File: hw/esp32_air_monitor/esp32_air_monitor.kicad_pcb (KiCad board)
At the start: 2 copper layers, 155 x 60 mm, 7 parts, among them J1 Conn_01x02_Male, J2 Connector_LED_matrix_64x32, J3 Connector_LED_matrix_64x32, J4 Connector_Pimoroni_BME280, J5 Connector_Adafruit_VEML7700, U1 ESP32-DEVKITC-32D, U2 SCD30

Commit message: :)s
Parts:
- moved J4 2.41 mm to (143.8, 116.4)
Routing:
- net +3V3: track 137.4 -> 142.7 mm
- net /SDA: track 93.6 -> 97.1 mm
- net /SCL: track 127.6 -> 130.4 mm
- net +5V: track 122.2 -> 123.3 mm

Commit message: :)
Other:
- board text added: "JLCJLCJLCJLC"

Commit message: Update PCB
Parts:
- added R1: 10k, Resistor_SMD:R_1206_3216Metric_Pad1.30x1.75mm_HandSolder, F.Cu at (133.0, 93.7)
- added R2: 10k, Resistor_SMD:R_1206_3216Metric_Pad1.30x1.75mm_HandSolder, F.Cu at (96.9, 93.4)
- added R3: 10k, Resistor_SMD:R_1206_3216Metric_Pad1.30x1.75mm_HandSolder, F.Cu at (130.5, 93.7)
- added R4: 10k, Resistor_SMD:R_1206_3216Metric_Pad1.30x1.75mm_HandSolder, F.Cu at (127.9, 93.7)
- added R5: 10k, Resistor_SMD:R_1206_3216Metric_Pad1.30x1.75mm_HandSolder, F.Cu at (125.4, 93.7)
- added R6: 10k, Resistor_SMD:R_1206_3216Metric_Pad1.30x1.75mm_HandSolder, F.Cu at (106.5, 93.4)
- added R7: 10k, Resistor_SMD:R_1206_3216Metric_Pad1.30x1.75mm_HandSolder, F.Cu at (115.8, 93.4)
- added SW1: SW_Push, qc_attiny:Push_Button_6x6mm, F.Cu at (96.9, 88.0)
- added SW2: SW_Push, qc_attiny:Push_Button_6x6mm, F.Cu at (106.5, 88.0)
- added SW3: SW_Push, qc_attiny:Push_Button_6x6mm, F.Cu at (115.8, 88.0)
- added SW4: SW_DIP_x04, Button_Switch_THT:SW_DIP_SPSTx04_Slide_9.78x12.34mm_W7.62mm_P2.54mm, F.Cu at (125.4, 89.2)
- moved J4 53.1 mm to (187.3, 86.0)
- moved J1 42.1 mm to (143.9, 85.5), turned to 90 degrees
- moved J5 14.0 mm to (165.6, 119.7)
- moved J3 2.54 mm to (215.1, 93.4)
- moved U1 0.79 mm to (108.9, 113.7), turned to 270 degrees
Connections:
- J2 pad 2: /MOSI -> /R0
- J2 pad 8: /B1 -> /MOSI
- J3 pad 1: /G1 -> /R0
- J3 pad 2: /R1 -> (no net)
- J3 pad 4: /B1 -> /G0
- J3 pad 5: /B0 -> /R1
- J3 pad 6: /G0 -> /B0
- J3 pad 8: (no net) -> /G1
- U1 pad 10: (no net) -> /BUT_2
- U1 pad 11: (no net) -> /BUT_1
- U1 pad 21: /LINE_A -> (no net)
- U1 pad 22: /LINE_B -> /SDA
- U1 pad 23: (no net) -> /SCL
- U1 pad 25: /LINE_C -> (no net)
- U1 pad 27: /LINE_D -> (no net)
- U1 pad 28: /LATCH -> /LINE_B
- U1 pad 29: (no net) -> /LINE_D
- U1 pad 31: /OE -> (no net)
- U1 pad 32: /SCL -> /LINE_A
- U1 pad 33: (no net) -> /LINE_C
- U1 pad 34: (no net) -> /LATCH
- U1 pad 35: /SDA -> /OE
- U1 pad 5: (no net) -> /DIP_4
- U1 pad 6: (no net) -> /DIP_3
- U1 pad 7: (no net) -> /DIP_2
- U1 pad 8: (no net) -> /DIP_1
- U1 pad 9: (no net) -> /BUT_3
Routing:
- net /R0: track 0.00 -> 171.6 mm
- net /B1: track 143.5 -> 0.00 mm
- net /MOSI: track 94.4 -> 18.0 mm
- net /R1: track 143.6 -> 196.5 mm
- net +5V: track 123.3 -> 79.9 mm
- net /SCLK: track 67.2 -> 30.5 mm
- net /LINE_A: track 15.8 -> 50.7 mm
- net /G1: track 143.6 -> 174.6 mm
- net /SCL: track 130.4 -> 106.5 mm
- net /B0: track 166.4 -> 190.2 mm
- net /SDA: track 97.1 -> 119.8 mm, vias 0 -> 1
- net /DIP_1: track 0.00 -> 22.2 mm, vias 0 -> 1
- net /LINE_B: track 17.0 -> 39.2 mm
- net /DIP_3: track 0.00 -> 21.8 mm, vias 0 -> 1
- net /DIP_4: track 0.00 -> 21.8 mm, vias 0 -> 1
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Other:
- board text added: "Bosch BME280 T, RH, p sensor"
- board text added: "ESP32 air quality monitor (T, RH, p, CO2, Ev) Jan Vrhovec, 2021"
- board text added: "Espressif ESP32 Microcontroller"
- board text added: "Sensirion SCD30 CO2 sensor"
- board text added: "Vishay VEML7700 Ambient light sensor"
- board text removed: "ESP32 Air Quality Monitor (T, RH, p, CO2) Jan Vrhovec, 2020"

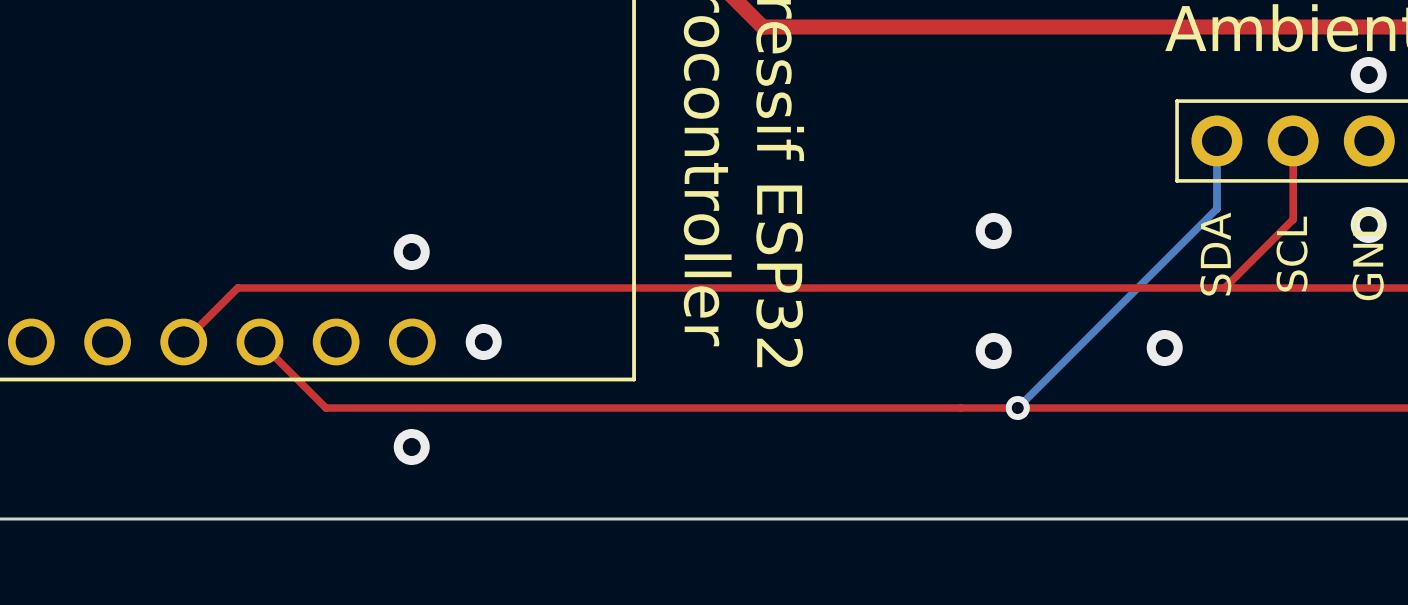
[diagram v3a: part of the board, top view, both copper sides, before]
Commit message: Fix hardware bug (SCL pin), patch software for new hw revision
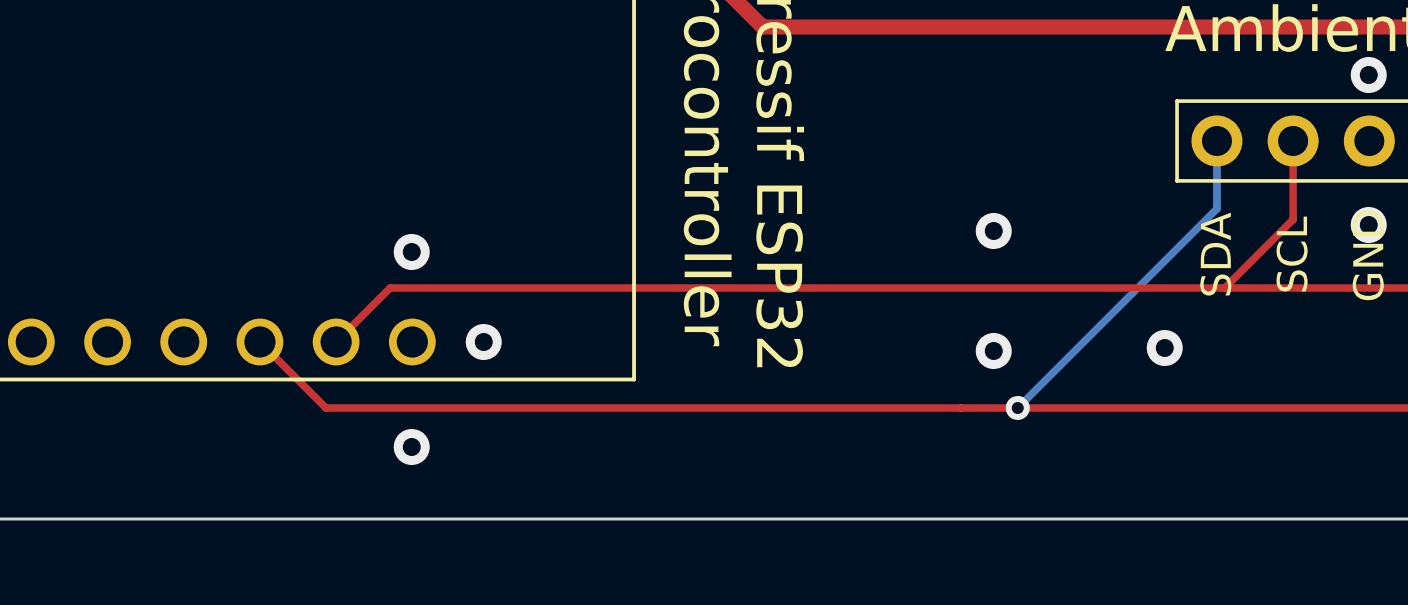
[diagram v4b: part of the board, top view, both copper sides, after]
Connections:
- U1 pad 21: (no net) -> /SCL
- U1 pad 23: /SCL -> (no net)
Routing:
- net /SCL: track 106.5 -> 101.4 mm
